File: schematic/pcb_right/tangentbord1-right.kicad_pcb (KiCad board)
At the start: 2 copper layers, 129 x 77.5 mm, 26 parts, among them J1 UART, J2 DBG

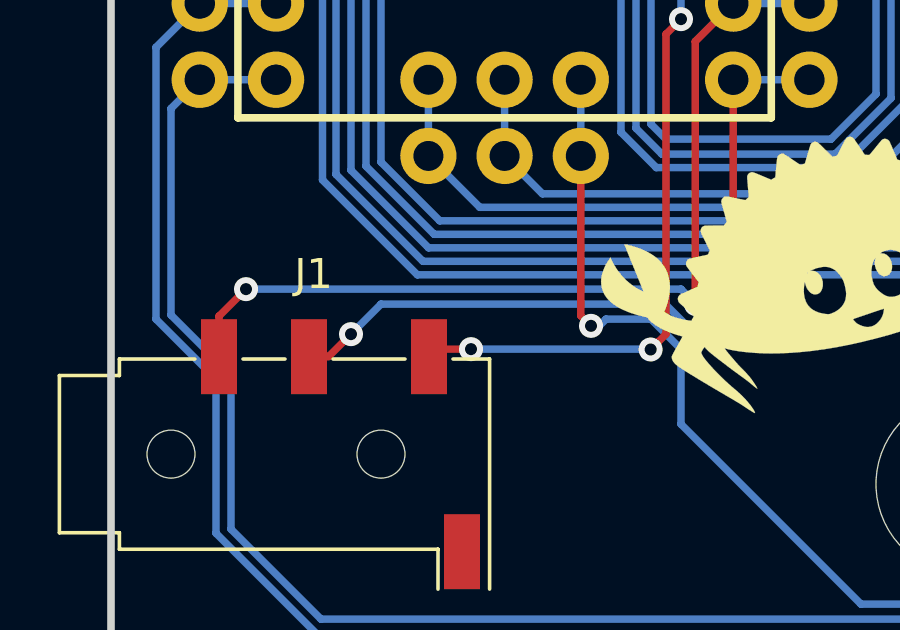
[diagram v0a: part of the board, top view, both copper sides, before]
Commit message: Swap RX/TX on pcb_right
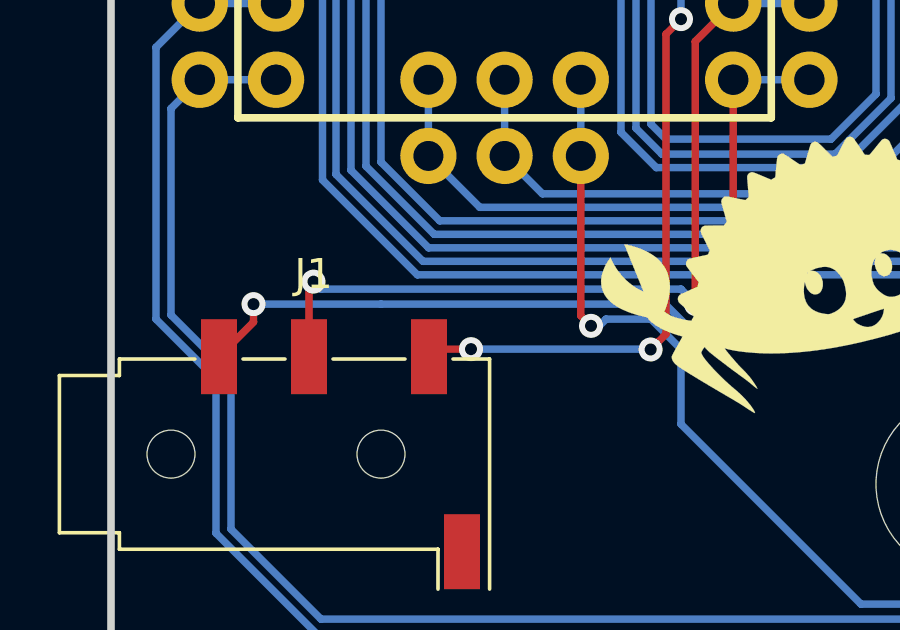
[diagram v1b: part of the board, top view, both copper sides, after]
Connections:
- J1 pad R1: /RX -> /TX
- J1 pad R2: /TX -> /RX
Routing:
- net /RX: track 25.4 -> 28.7 mm
- net /TX: track 30.9 -> 28.7 mm
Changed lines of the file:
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@@
     (pad "" np_thru_hole circle (at 2.25 0) (size 1.6 1.6) (drill 1.6) (layers "F&B.Cu" "*.Mask"))
     (pad "R1" smd rect (at -0.15 -3.25) (size 1.2 2.5) (layers "F.Cu" "F.Paste" "F.Mask")
-      (net 28 "/RX") (pintype "passive"))
-    (pad "R2" smd rect (at -3.15 -3.25) (size 1.2 2.5) (layers "F.Cu" "F.Paste" "F.Mask")
       (net 29 "/TX") (pintype "passive"))
+    (pad "R2" smd rect (at -3.15 -3.25) (size 1.2 2.5) (layers "F.Cu" "F.Paste" "F.Mask")
+      (net 28 "/RX") (pintype "passive"))
     (pad "S" smd rect (at 4.95 3.25) (size 1.2 2.5) (layers "F.Cu" "F.Paste" "F.Mask")
       (net 1 "GND") (pintype "passive"))
@@
   (segment (start 132 40.5) (end 139.142 47.642) (width 0.25) (layer "B.Cu") (net 27))
   (segment (start 101 38) (end 117 38) (width 0.25) (layer "B.Cu") (net 27))
-  (segment (start 34.6 72.75) (end 35.25 72.75) (width 0.25) (layer "F.Cu") (net 28))
-  (segment (start 35.25 72.75) (end 36 72) (width 0.25) (layer "F.Cu") (net 28))
+  (segment (start 32.75 71.6) (end 31.6 72.75) (width 0.25) (layer "F.Cu") (net 28))
+  (segment (start 32.75 71) (end 32.75 71.6) (width 0.25) (layer "F.Cu") (net 28))
   (segment (start 48.74 70.76) (end 48.5 71) (width 0.25) (layer "F.Cu") (net 28))
   (segment (start 48.74 63.52) (end 48.74 70.76) (width 0.25) (layer "F.Cu") (net 28))
-  (via (at 36 72) (size 0.8) (drill 0.4) (layers "F.Cu" "B.Cu") (net 28))
+  (via (at 32.75 71) (size 0.8) (drill 0.4) (layers "F.Cu" "B.Cu") (net 28))
   (via (at 48.5 71) (size 0.8) (drill 0.4) (layers "F.Cu" "B.Cu") (net 28))
-  (segment (start 36 72) (end 37 71) (width 0.25) (layer "B.Cu") (net 28))
   (segment (start 46.5 71) (end 37 71) (width 0.25) (layer "B.Cu") (net 28))
   (segment (start 47.800305 71.725) (end 47.199695 71.725) (width 0.25) (layer "B.Cu") (net 28))
   (segment (start 48.5 71) (end 48.5 71.025305) (width 0.25) (layer "B.Cu") (net 28))
   (segment (start 48.74 63.52) (end 51.28 63.52) (width 0.25) (layer "B.Cu") (net 28))
+  (segment (start 37 71) (end 32.75 71) (width 0.25) (layer "B.Cu") (net 28))
   (segment (start 48.5 71.025305) (end 47.800305 71.725) (width 0.25) (layer "B.Cu") (net 28))
   (segment (start 46.5 71.025305) (end 46.5 71) (width 0.25) (layer "B.Cu") (net 28))
   (segment (start 47.199695 71.725) (end 46.5 71.025305) (width 0.25) (layer "B.Cu") (net 28))
-  (segment (start 31.6 71.4) (end 32.5 70.5) (width 0.25) (layer "F.Cu") (net 29))
   (segment (start 47.475 62.245) (end 48.74 60.98) (width 0.25) (layer "F.Cu") (net 29))
   (segment (start 47.475 62.245) (end 47.475 70.975) (width 0.25) (layer "F.Cu") (net 29))
+  (segment (start 34.6 70.4) (end 34.6 72.75) (width 0.25) (layer "F.Cu") (net 29))
   (segment (start 47.475 70.975) (end 47.5 71) (width 0.25) (layer "F.Cu") (net 29))
-  (segment (start 31.6 72.75) (end 31.6 71.4) (width 0.25) (layer "F.Cu") (net 29))
+  (segment (start 34.75 70.25) (end 34.6 70.4) (width 0.25) (layer "F.Cu") (net 29))
   (via (at 47.5 71) (size 0.8) (drill 0.4) (layers "F.Cu" "B.Cu") (net 29))
-  (via (at 32.5 70.5) (size 0.8) (drill 0.4) (layers "F.Cu" "B.Cu") (net 29))
+  (via (at 34.75 70.25) (size 0.8) (drill 0.4) (layers "F.Cu" "B.Cu") (net 29))
   (segment (start 51.28 60.98) (end 48.74 60.98) (width 0.25) (layer "B.Cu") (net 29))
+  (segment (start 47 70.5) (end 35 70.5) (width 0.25) (layer "B.Cu") (net 29))
   (segment (start 47.5 71) (end 47 70.5) (width 0.25) (layer "B.Cu") (net 29))
-  (segment (start 32.5 70.5) (end 47 70.5) (width 0.25) (layer "B.Cu") (net 29))
+  (segment (start 35 70.5) (end 34.75 70.25) (width 0.25) (layer "B.Cu") (net 29))
   (segment (start 92.5 80) (end 93.5 79) (width 0.25) (layer "B.Cu") (net 30))
   (segment (start 33.5 60.98) (end 30.96 60.98) (width 0.25) (layer "B.Cu") (net 30))
